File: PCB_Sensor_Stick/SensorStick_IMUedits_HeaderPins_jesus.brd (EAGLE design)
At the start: 63.5 x 38.1 mm, 49 parts, among them IC1 SAM-M8Q-0-10, IC2 STM32L412RBT6P, IC3 DPS310XTSA1, IC5 BMI085, IC6 IIS2MDCTR, J1 USB4160-03-0230-C, U1 4525DO-DS5AI001DP, U2 LD39050PU33R

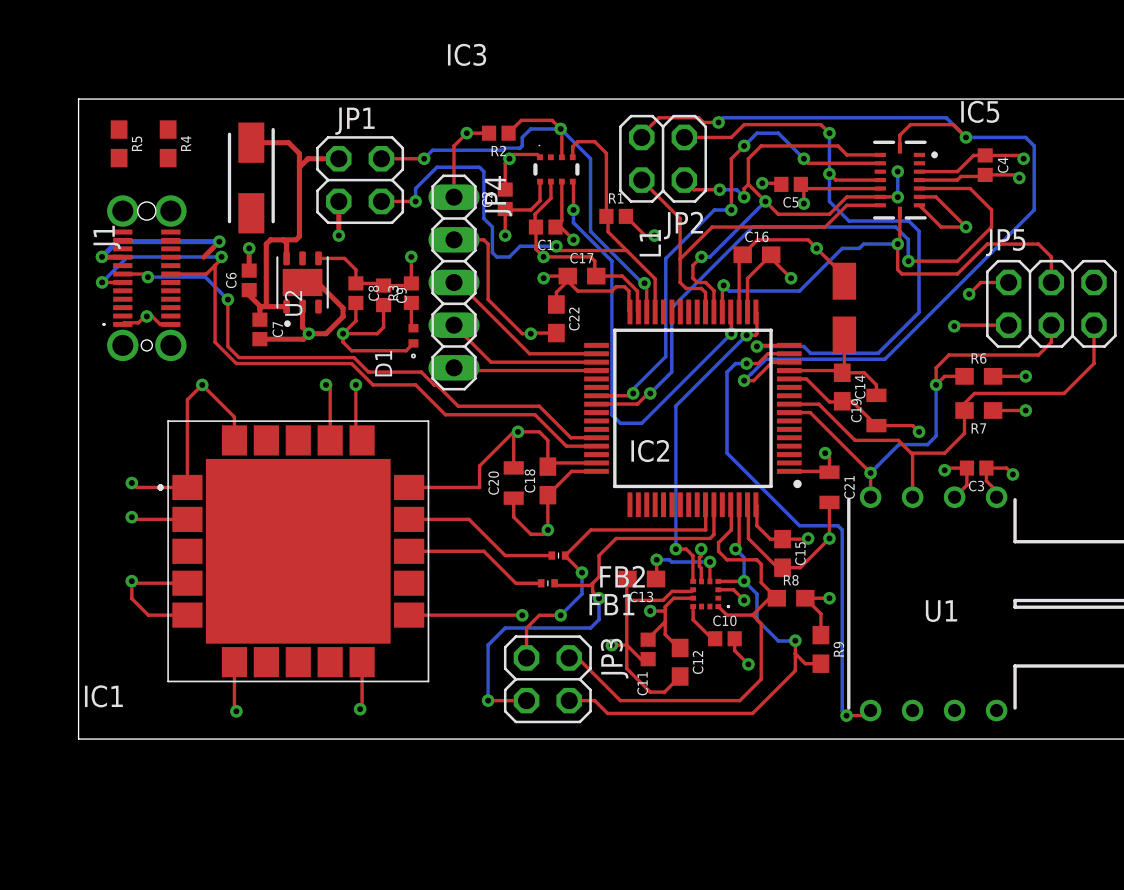
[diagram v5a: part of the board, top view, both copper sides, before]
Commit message: Added in JST connection and renamed all sensors
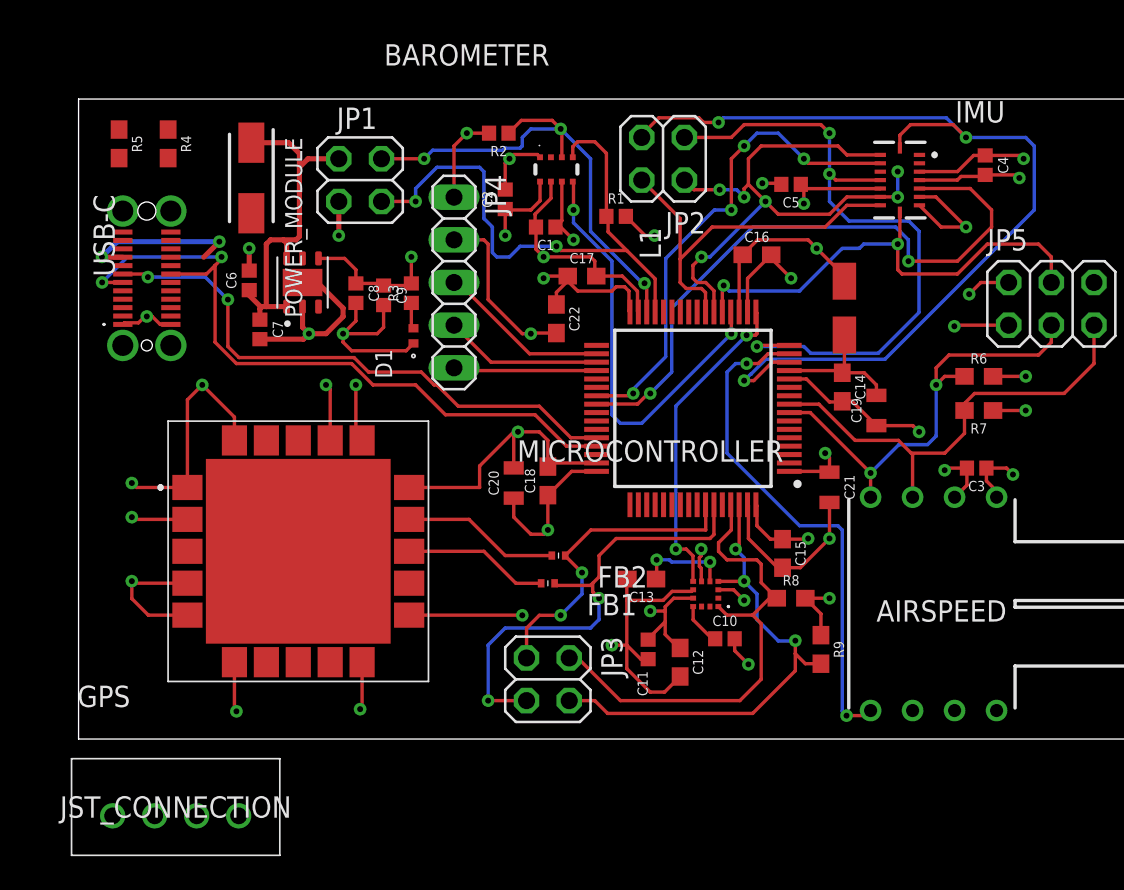
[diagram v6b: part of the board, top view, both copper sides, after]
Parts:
- added JST_CONNECTION: B4B-XH-A_LF__SN_, B4B-XH-A_LF__SN_:B4BXHALFSN
- renumbered IC1 to GPS, IC2 to MICROCONTROLLER, IC3 to BAROMETER, IC5 to IMU, IC6 to MAGNETOMETER, J1 to USB-C, U1 to AIRSPEED, U2 to POWER_MODULE
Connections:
- net 5V: now also JST_CONNECTION.1
- net GND: now also JST_CONNECTION.4
- net USB_DN: now also JST_CONNECTION.3
- net USB_DP: now also JST_CONNECTION.2

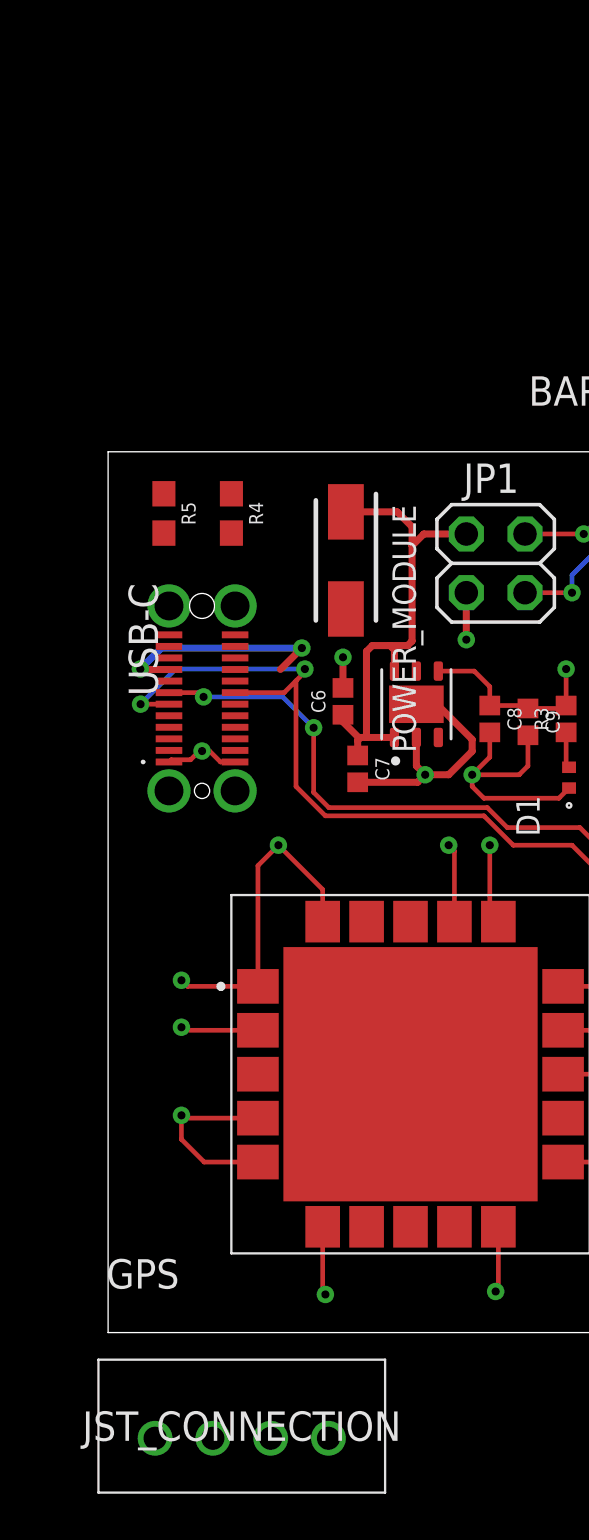
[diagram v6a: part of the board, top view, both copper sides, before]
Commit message: J - Removed USB-C connector, wired JST-XH connector, PCB/Schematic first draft
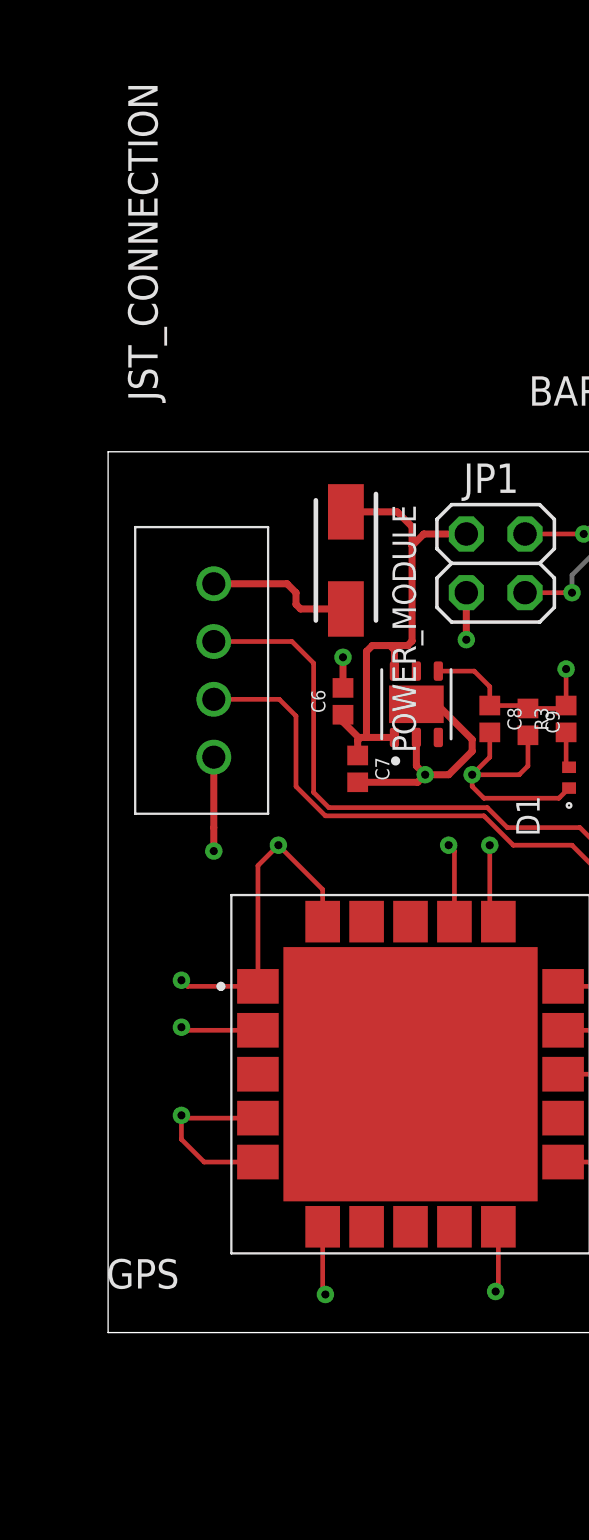
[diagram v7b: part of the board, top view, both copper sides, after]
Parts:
- removed R4, R5: 1.5k, SparkFun-Resistors:0603
- removed USB-C: USB4160-03-0230-C, USB4160-03-0230-C:USB4160030230C
- moved JST_CONNECTION 29.6 mm to (4.57, 24.9), turned to 90 degrees
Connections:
- removed net N$10: R4.2, USB-C.B5
- removed net N$3: R5.2, USB-C.A5
- net 5V: no longer JST_CONNECTION.1
- net 5V_IN: now also JST_CONNECTION.4; no longer USB-C.A4, USB-C.A9, USB-C.B4, USB-C.B9
- net GND: now also JST_CONNECTION.1; no longer JST_CONNECTION.4, R4.1, R5.1, USB-C.A1, USB-C.A12, USB-C.B1, USB-C.B12, USB-C.MH1, USB-C.MH2, USB-C.MH3, USB-C.MH4
- net USB_DN: no longer USB-C.A7, USB-C.B7
- net USB_DP: no longer USB-C.A6, USB-C.B6
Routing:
- net USB_DP: track 42.3 -> 32.2 mm, vias 2 -> 0
- net 5V_IN: track 9.93 -> 6.46 mm, vias 2 -> 0
- net GND: track 179.9 -> 180.7 mm
- net USB_DN: track 33.9 -> 34.5 mm, vias 2 -> 0

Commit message: J - Updates based off of Phil feedback
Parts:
- added JP6: (no value), pinhead:1X06
- added R10: 0, SparkFun-Resistors:0603
- added R5: 10k, SparkFun-Resistors:0603
- added S1: LL3301FF065QJ, ce-capstone:LL3301FF065QJ
- added U1: ECMF02-4CMX8, ECMF02-4CMX8:MICRO_QFN-8L_STM
- added U2: TPD6F003DQDR, TPD6F003DQDR:DQD12_2X0P4
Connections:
- removed net N$6: C10.1, MAGNETOMETER.10
- new net BOOT0: MICROCONTROLLER.60, R5.1, S1.3, S1.4
- new net DN: JST_CONNECTION.3, U1.2
- new net DP: JST_CONNECTION.2, U1.3
- new net NRST: GPS.18, MICROCONTROLLER.7, POWER_MODULE.3, U2.4
- new net NRST_O: JP6.4, U2.9
- new net RX_O: JP6.5, U2.8
- new net SWCLK: MICROCONTROLLER.49, U2.2
- new net SWCLK_O: JP6.2, U2.11
- new net SWDIO: MICROCONTROLLER.46, U2.3
- new net SWDIO_O: JP6.3, U2.10
- new net SWO: MICROCONTROLLER.55, U2.1
- new net SWO_O: JP6.1, U2.12
- new net TX_O: JP6.6, U2.7
- net 3V3: now also BAROMETER.2, BAROMETER.5, C10.1, GPS.3, MAGNETOMETER.10, MAGNETOMETER.3, S1.1, S1.2, U1.1
- net GND: now also R5.2, U1.5, U1.8, U2.13; no longer MAGNETOMETER.3
- net GPIO_EXTI2: now also R10.1
- net GPIO_EXTI4: now also IMU.1, R10.2; no longer BAROMETER.5
- net USART3_RX: now also U2.5
- net USART3_TX: now also U2.6
- net USB_DN: now also U1.7; no longer JST_CONNECTION.3
- net USB_DP: now also U1.6; no longer JST_CONNECTION.2
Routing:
- net 3V3: track 104.1 -> 108.4 mm, vias 20 -> 21
- net USB_DN: track 34.5 -> 31.1 mm
- net USB_DP: track 32.2 -> 29.3 mm
- net N$6: track 2.57 -> 0.00 mm
- net GND: track 180.7 -> 178.9 mm, vias 28 -> 27
